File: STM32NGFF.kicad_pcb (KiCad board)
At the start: 2 copper layers, 30 parts, among them J1 USB_C_Receptacle_USB2.0, J2 2199119-4, U1 MIC5205-3.3YM5, U2 STM32F303CCTx, U3 USBLC6-2SC6, Y1 16MHz

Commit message: Routed and shaped PCB
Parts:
- added C13: 10n, Capacitor_SMD:C_0603_1608Metric, F.Cu at (215.3, 89.0)
- added C14: 10uf, Capacitor_SMD:C_0603_1608Metric, F.Cu at (254.0, 96.0)
- added J3: HRO_TYPE-C-31-M-12, Type-C:HRO-TYPE-C-31-M-12-Assembly, F.Cu at (259.2, 84.8)
- added J4: S4B-PH-K-S(LF)(SN), JST:S4B-PH-K-S_LF_SN, F.Cu at (259.4, 102.2)
- added R7: 5.11k, Capacitor_SMD:C_0603_1608Metric, F.Cu at (259.6, 96.0)
- added R8: 1M, Capacitor_SMD:C_0603_1608Metric, F.Cu at (253.2, 89.4)
- added REF**: MountingHole_2.2mm_M2, MountingHole:MountingHole_2.2mm_M2, F.Cu at (268.8, 89.4)
- added REF**: MountingHole_2.2mm_M2, MountingHole:MountingHole_2.2mm_M2, F.Cu at (268.8, 105.6)
- added REF**: MountingHole_2.2mm_M2, MountingHole:MountingHole_2.2mm_M2, F.Cu at (249.8, 105.6)
- added REF**: MountingHole_2.2mm_M2, MountingHole:MountingHole_2.2mm_M2, F.Cu at (249.8, 89.4)
- added U4: USBLC6-2SC6, Package_TO_SOT_SMD:SOT-23-6, F.Cu at (262.4, 96.4)
- C12: value 10n -> 100nF
- C3: value 10uf -> 2.2uF
- C4: value 2.2uF -> 4u7
- C5: value 4u7 -> 100n
- C6: value 100nF -> 100n
- C7: value 100n -> 100nF
- J1: value USB_C_Receptacle_USB2.0 -> NASMO-S6701-TP40; footprint Connector_USB:USB_C_Receptacle_HRO_TYPE-C-31-M-12 -> Argosy Research:NASMO-S6701-TP40
- J2: value 2199119-4 -> S4B-PH-K-S(LF)(SN); footprint TE:TE_2199119-4 -> JST:S4B-PH-K-S_LF_SN
- R4: value 1M -> 470
- R5: value 5.11k -> 1M
- U1: value MIC5205-3.3YM5 -> 74LVC1G17
- U2: value STM32F303CCTx -> MIC5205-3.3YM5; footprint Package_QFP:LQFP-48_7x7mm_P0.5mm -> Package_TO_SOT_SMD:SOT-23-5
- U3: value USBLC6-2SC6 -> STM32F303RBTx; footprint Package_TO_SOT_SMD:SOT-23-6 -> Package_QFP:LQFP-64_10x10mm_P0.5mm
- moved FB1 117.6 mm to (255.8, 96.2), turned to 90 degrees
- moved R6 111.0 mm to (265.2, 96.0), turned to 270 degrees
- moved C12 110.4 mm to (265.2, 89.4), turned to 90 degrees
- moved F1 94.3 mm to (257.8, 96.4), turned to 90 degrees
- moved C11 94.3 mm to (215.3, 87.5)
- moved C10 90.4 mm to (210.7, 83.8)
- moved U1 83.6 mm to (210.2, 94.1)
- moved L1 82.4 mm to (215.3, 90.7), turned to 180 degrees
- moved PSW1 80.0 mm to (193.6, 76.7), turned to 90 degrees
- moved R1 78.4 mm to (218.4, 84.8), turned to 90 degrees
- moved C3 77.7 mm to (215.3, 93.8), turned to 180 degrees
- moved U3 75.6 mm to (201.1, 83.9), turned to 45 degrees
- moved C5 75.0 mm to (190.9, 83.5), turned to 135 degrees
- moved C8 73.5 mm to (201.1, 75.5), turned to 180 degrees
- moved R5 72.7 mm to (216.0, 101.6), turned to 270 degrees
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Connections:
- C12 pad 1: +3.3VA -> Net-(C12-Pad1)
- C3 pad 2: +5V -> +3V3
- C4 pad 1: GND -> +3V3
- C4 pad 2: +3V3 -> GND
- C6 pad 1: Net-(C6-Pad1) -> +3V3
- C7 pad 1: +3V3 -> Net-(C7-Pad1)
- D2 pad 2: LED_STATUS -> /LED_STATUS
- F1 pad 2: Net-(F1-Pad2) -> /VBUS
- J2 pad 1: +3V3 -> +5V
- J2 pad 2: Net-(J2-Pad2) -> /USB_D-
- J2 pad 3: GND -> /USB_D+
- J2 pad 4: Net-(J2-Pad4) -> GND
- R4 pad 1: Net-(C6-Pad1) -> /LED_DATA
- R4 pad 2: GND -> /LED_5V
- R5 pad 1: Net-(J1-PadA5) -> Net-(C7-Pad1)
- R6 pad 1: Net-(J1-PadB5) -> Net-(J3-Pad4)
- U1 pad 1: +5V -> (no net)
- U1 pad 2: GND -> /LED_3V3
- U1 pad 3: +5V -> GND
- U1 pad 4: Net-(U1-Pad4) -> /LED_5V
- U1 pad 5: +3V3 -> +5V
- U2 pad 1: +3V3 -> +5V
- U2 pad 2: /PC3 -> GND
- U2 pad 3: PC14 -> +5V
- U2 pad 4: PC15 -> Net-(U2-Pad4)
- U2 pad 5: /HF_XTAL_P -> +3V3
- U3 pad 1: USB_CONN_D- -> +3V3
- U3 pad 2: GND -> /PC13
- U3 pad 3: USB_CONN_D+ -> /PC14
- U3 pad 4: USB_D+ -> /PC15
- U3 pad 5: +5V -> /HF_XTAL_P
- U3 pad 6: USB_D- -> /HF_XTAL_N
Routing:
- net +3V3: track 0.00 -> 118.2 mm, vias 0 -> 5
- net +5V: track 0.00 -> 62.4 mm, vias 0 -> 3
- net GND: track 0.00 -> 60.5 mm, vias 0 -> 28
- net /PA14: track 0.00 -> 31.5 mm, vias 0 -> 2
- net /PA15: track 0.00 -> 31.1 mm, vias 0 -> 2
- net /PC10: track 0.00 -> 30.7 mm, vias 0 -> 2
- net /PA13: track 0.00 -> 30.5 mm, vias 0 -> 2
- net /PC11: track 0.00 -> 30.3 mm, vias 0 -> 2
- net /PC12: track 0.00 -> 29.8 mm, vias 0 -> 2
- net /PA10: track 0.00 -> 29.7 mm, vias 0 -> 2
- net /PD2: track 0.00 -> 29.4 mm, vias 0 -> 2
- net /PA9: track 0.00 -> 29.4 mm, vias 0 -> 2
- net /PA8: track 0.00 -> 28.9 mm, vias 0 -> 2
- net /PB3: track 0.00 -> 28.9 mm, vias 0 -> 2
- net Net-(C7-Pad1): track 0.00 -> 28.7 mm
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- added copper zone on B.Cu, net GND
- added copper zone on F.Cu, net GND
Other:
- board outline added: 87 x 38.9 mm
- net class Default: clearance 0.2 -> 0.127
- rule trace_clearance: 0.2 -> 0.127
- rule trace_min: 0.2 -> 0.127
- rule via_min_drill: 0.3 -> 0.2
- rule via_min_size: 0.4 -> 0.45

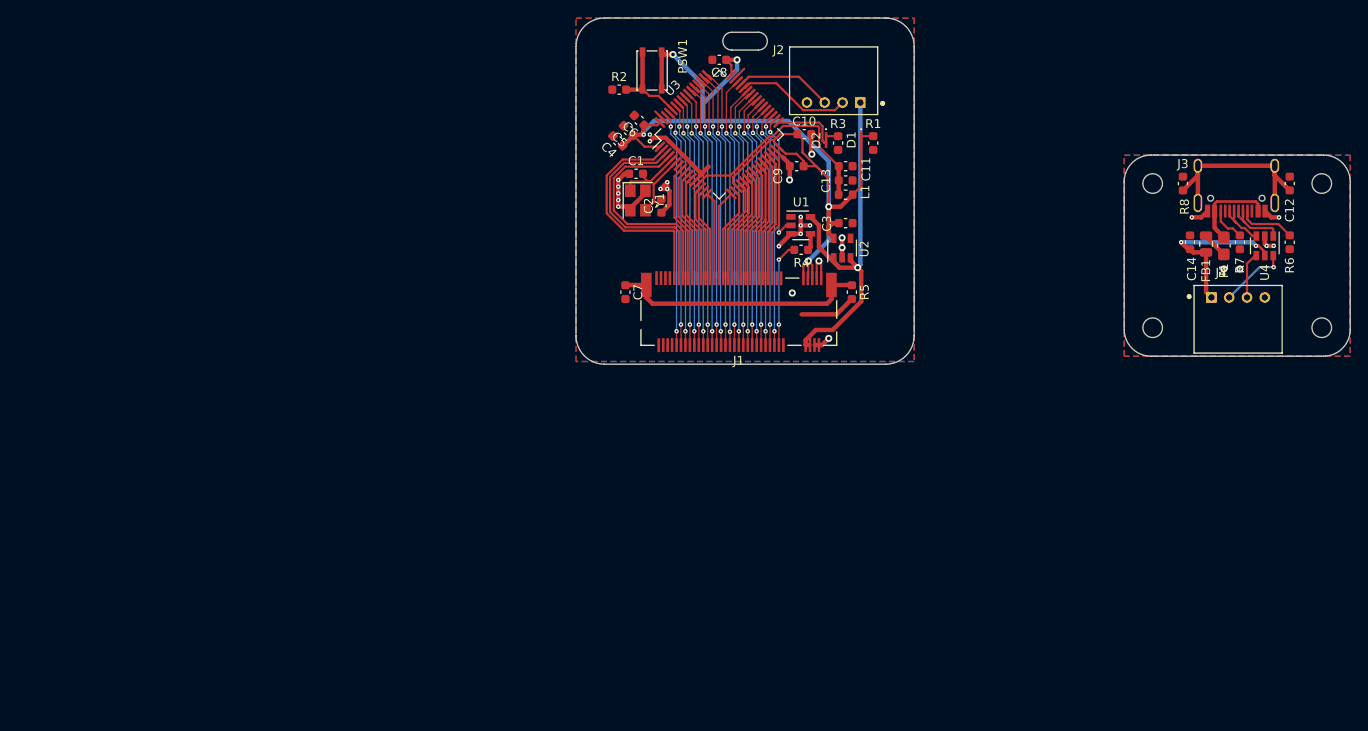
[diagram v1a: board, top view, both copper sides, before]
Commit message: Updated images
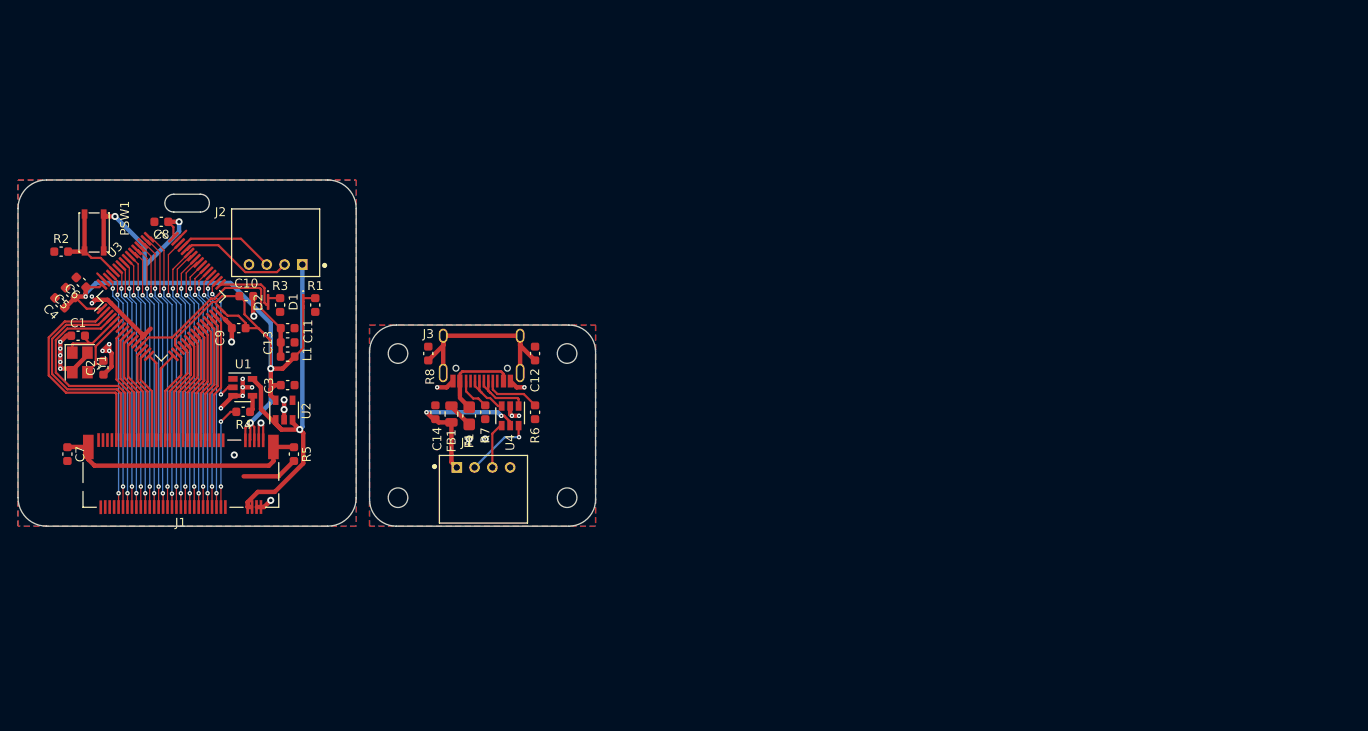
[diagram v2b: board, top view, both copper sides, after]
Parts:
- moved C14 86.9 mm to (169.2, 115.1)
- moved F1 86.9 mm to (173.0, 115.5)
- moved FB1 86.9 mm to (171.0, 115.3)
- moved R7 86.9 mm to (174.8, 115.1)
- moved REF** 86.9 mm to (184.0, 108.5)
- moved REF** 86.9 mm to (184.0, 124.7)
- moved REF** 86.9 mm to (165.0, 124.7)
- moved REF** 86.9 mm to (165.0, 108.5)
- moved C12 86.9 mm to (180.4, 108.5)
- moved J3 86.9 mm to (174.4, 103.9)
- moved J4 86.9 mm to (174.6, 121.3)
- moved R6 86.9 mm to (180.4, 115.1)
- moved R8 86.9 mm to (168.4, 108.5)
- moved U4 86.9 mm to (177.6, 115.5)
- moved C10 65.3 mm to (147.9, 102.0)
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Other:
- board size 87 x 38.9 mm -> 64.9 x 38.9 mm
